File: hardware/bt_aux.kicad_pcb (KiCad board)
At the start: 2 copper layers, 52 x 28 mm, 18 parts, among them J1 esp32_1, J2 esp32_2, J3 audio_out, U1 PCM5102A

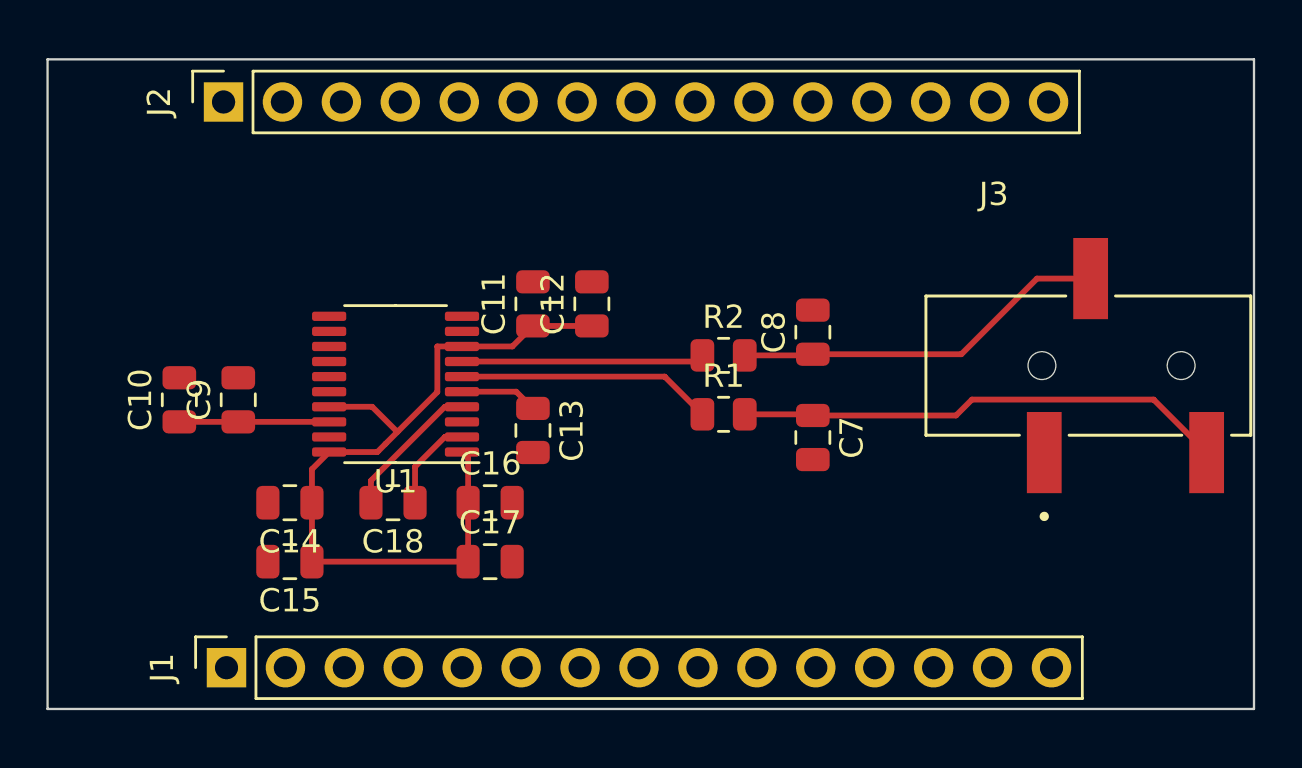
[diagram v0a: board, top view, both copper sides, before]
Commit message: add copper pours and rest of connections to headers
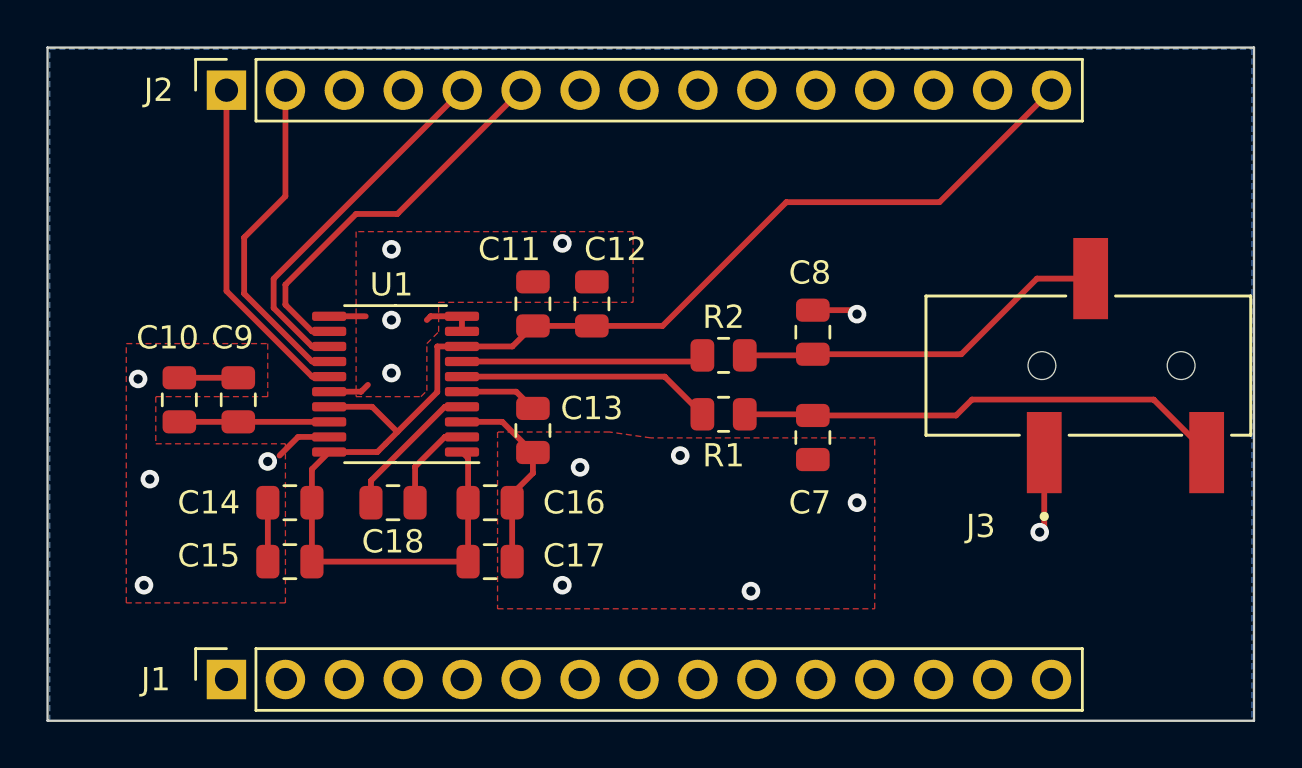
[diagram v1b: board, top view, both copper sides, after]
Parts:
- moved J2 0.52 mm to (127.8, 91.4)
- moved J1 0.51 mm to (127.8, 116.8)
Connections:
- J1 pad 10: /lrck -> unconnected-(J1-Pin_10-Pad10)
- J1 pad 11: /din -> unconnected-(J1-Pin_11-Pad11)
- J1 pad 12: /bck -> unconnected-(J1-Pin_12-Pad12)
- J1 pad 13: /sck -> unconnected-(J1-Pin_13-Pad13)
- J2 pad 1: unconnected-(J2-Pin_1-Pad1) -> /lrck
- J2 pad 2: unconnected-(J2-Pin_2-Pad2) -> /din
- J2 pad 5: unconnected-(J2-Pin_5-Pad5) -> /bck
- J2 pad 6: unconnected-(J2-Pin_6-Pad6) -> /sck
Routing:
- net GND: track 0.00 -> 27.3 mm, vias 0 -> 15
- net +3.3V: track 34.7 -> 58.7 mm
- net /sck: track 0.00 -> 16.9 mm
- net /bck: track 0.00 -> 15.8 mm
- net /lrck: track 0.00 -> 14.6 mm
- net /din: track 0.00 -> 14.4 mm
- added copper zone on B.Cu, net GND
- added copper zone on F.Cu, net GND
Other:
- board size 52 x 28 mm -> 52 x 29 mm

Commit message: give pcb nice beautiful corners
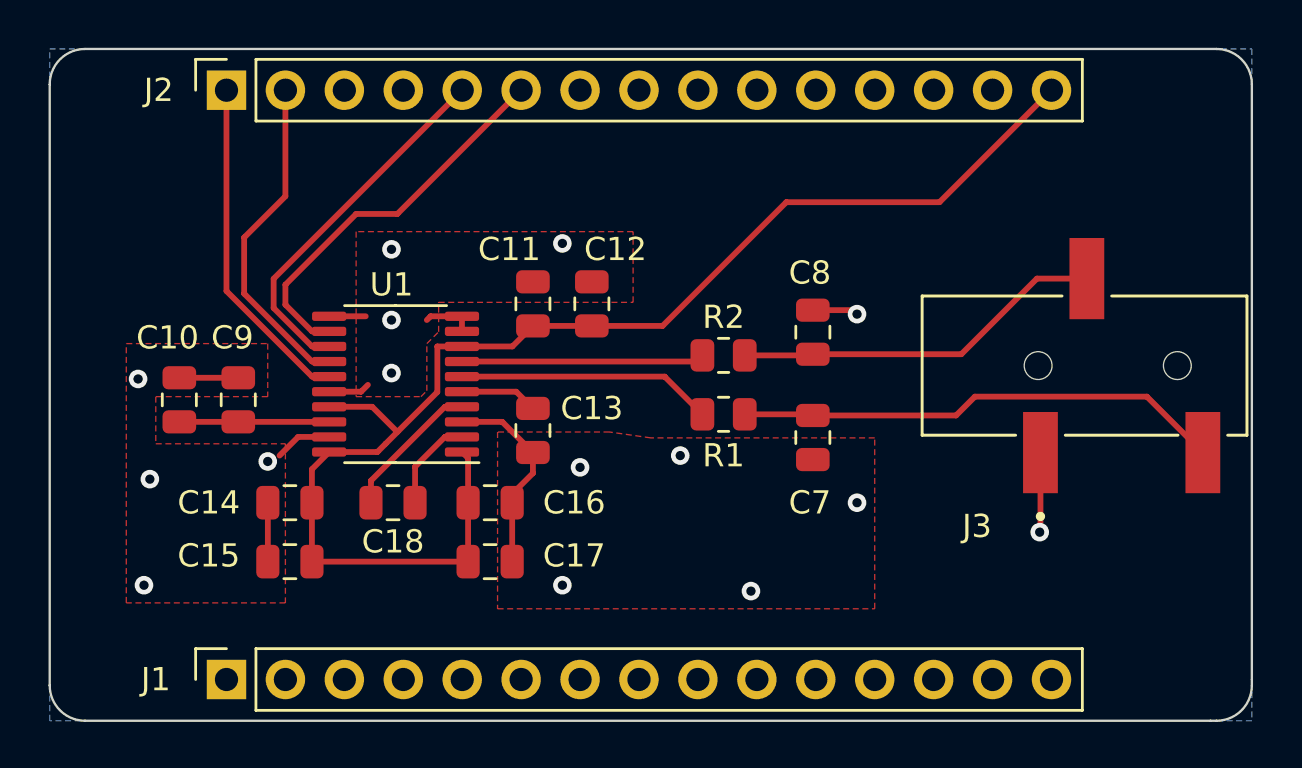
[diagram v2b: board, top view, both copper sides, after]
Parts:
- moved J3 0.16 mm to (165.7, 103.3)
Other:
- board size 52 x 29 mm -> 51.8 x 29 mm
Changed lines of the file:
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@@
   )
   (footprint "audio-jack:BOOMELE_PJ-320B" (layer "F.Cu")
-    (at 165.91 103.31)
+    (at 165.746 103.31)
     (property "Link" "https://jlcpcb.com/partdetail/boomele_boom_Precision_elec-C18594/C18594")
     (property "Sheetfile" "bt_aux.kicad_sch")
@@
     )
   )
-  (gr_rect (start 120.05 89.602) (end 172.05 118.618)
-    (stroke (width 0.1) (type default)) (fill none) (layer "Edge.Cuts"))
-  (segment (start 159.893 104.775) (end 167.725 104.775) (width 0.25) (layer "F.Cu") (net 1))
+  (gr_line (start 170.18 118.618) (end 170.434 118.618)
+    (stroke (width 0.1) (type default)) (layer "Edge.Cuts"))
+  (gr_arc (start 170.434 89.662) (mid 171.511631 90.108369) (end 171.958 91.186)
+    (stroke (width 0.1) (type default)) (layer "Edge.Cuts"))
+  (gr_line (start 170.434 89.662) (end 121.666 89.662)
+    (stroke (width 0.1) (type default)) (layer "Edge.Cuts"))
+  (gr_line (start 171.958 116.84) (end 171.958 117.094)
+    (stroke (width 0.1) (type default)) (layer "Edge.Cuts"))
+  (gr_line (start 120.142 91.186) (end 120.142 117.094)
+    (stroke (width 0.1) (type default)) (layer "Edge.Cuts"))
+  (gr_line (start 121.666 118.618) (end 170.18 118.618)
+    (stroke (width 0.1) (type default)) (layer "Edge.Cuts"))
+  (gr_arc (start 121.666 118.618) (mid 120.588369 118.171631) (end 120.142 117.094)
+    (stroke (width 0.1) (type default)) (layer "Edge.Cuts"))
+  (gr_line (start 171.958 116.84) (end 171.958 91.186)
+    (stroke (width 0.1) (type default)) (layer "Edge.Cuts"))
+  (gr_arc (start 120.142 91.186) (mid 120.588369 90.108369) (end 121.666 89.662)
+    (stroke (width 0.1) (type default)) (layer "Edge.Cuts"))
+  (gr_arc (start 171.958 117.094) (mid 171.511631 118.171631) (end 170.434 118.618)
+    (stroke (width 0.1) (type default)) (layer "Edge.Cuts"))
   (segment (start 152.985 105.41) (end 153.035 105.46) (width 0.25) (layer "F.Cu") (net 1))
+  (segment (start 167.434 104.648) (end 169.846 107.06) (width 0.25) (layer "F.Cu") (net 1))
   (segment (start 150.1 105.41) (end 152.985 105.41) (width 0.25) (layer "F.Cu") (net 1))
+  (segment (start 160.02 104.648) (end 167.434 104.648) (width 0.25) (layer "F.Cu") (net 1))
+  (segment (start 159.208 105.46) (end 160.02 104.648) (width 0.25) (layer "F.Cu") (net 1))
   (segment (start 153.035 105.46) (end 159.208 105.46) (width 0.25) (layer "F.Cu") (net 1))
-  (segment (start 159.208 105.46) (end 159.893 104.775) (width 0.25) (layer "F.Cu") (net 1))
-  (segment (start 167.725 104.775) (end 170.01 107.06) (width 0.25) (layer "F.Cu") (net 1))
   (segment (start 139.649 105.735) (end 137.9125 105.735) (width 0.25) (layer "F.Cu") (net 2))
+  (segment (start 162.846 110.458) (end 162.814 110.49) (width 0.25) (layer "F.Cu") (net 2))
   (segment (start 140.076 108.844) (end 140.97 107.95) (width 0.25) (layer "F.Cu") (net 2))
   (segment (start 128.27 103.835) (end 125.73 103.835) (width 0.25) (layer "F.Cu") (net 2))
   (segment (start 153.035 100.92) (end 154.768 100.92) (width 0.25) (layer "F.Cu") (net 2))
+  (segment (start 162.846 107.06) (end 162.846 110.458) (width 0.25) (layer "F.Cu") (net 2))
   (segment (start 137.9125 101.185) (end 137.9125 101.835) (width 0.25) (layer "F.Cu") (net 2))
   (segment (start 140.076 109.22) (end 140.076 108.844) (width 0.25) (layer "F.Cu") (net 2))
@@
   (segment (start 132.1875 106.385) (end 130.851 106.385) (width 0.25) (layer "F.Cu") (net 2))
   (segment (start 140.97 107.056) (end 139.649 105.735) (width 0.25) (layer "F.Cu") (net 2))
-  (segment (start 163.01 107.06) (end 163.01 110.294) (width 0.25) (layer "F.Cu") (net 2))
   (via (at 142.24 112.776) (size 0.8) (drill 0.4) (layers "F.Cu" "B.Cu") (free) (net 2))
   (via (at 124.206 112.776) (size 0.8) (drill 0.4) (layers "F.Cu" "B.Cu") (free) (net 2))
@@
   (via (at 154.94 101.092) (size 0.8) (drill 0.4) (layers "F.Cu" "B.Cu") (net 2))
   (via (at 134.874 101.346) (size 0.8) (drill 0.4) (layers "F.Cu" "B.Cu") (free) (net 2))
+  (segment (start 162.695 99.56) (end 164.846 99.56) (width 0.25) (layer "F.Cu") (net 3))
   (segment (start 153.035 102.82) (end 159.435 102.82) (width 0.25) (layer "F.Cu") (net 3))
   (segment (start 150.1 102.87) (end 152.985 102.87) (width 0.25) (layer "F.Cu") (net 3))
+  (segment (start 152.985 102.87) (end 153.035 102.82) (width 0.25) (layer "F.Cu") (net 3))
   (segment (start 159.435 102.82) (end 162.695 99.56) (width 0.25) (layer "F.Cu") (net 3))
-  (segment (start 152.985 102.87) (end 153.035 102.82) (width 0.25) (layer "F.Cu") (net 3))
-  (segment (start 162.695 99.56) (end 165.01 99.56) (width 0.25) (layer "F.Cu") (net 3))
   (segment (start 128.265 105.405) (end 128.27 105.41) (width 0.25) (layer "F.Cu") (net 4))
   (segment (start 128.27 105.735) (end 125.73 105.735) (width 0.25) (layer "F.Cu") (net 4))
@@
     (connect_pads (clearance 0.5))
     (min_thickness 0.25) (filled_areas_thickness no)
-    (fill yes (thermal_gap 0.5) (thermal_bridge_width 0.5))
+    (fill yes (thermal_gap 0.5) (thermal_bridge_width 0.5) (smoothing fillet) (radius 1.524) (island_removal_mode 1) (island_area_min 10))
     (polygon
       (pts
-        (xy 171.958 89.662)
         (xy 171.958 118.618)
         (xy 120.142 118.618)
         (xy 120.142 89.662)
+        (xy 171.958 89.662)
       )
     )
